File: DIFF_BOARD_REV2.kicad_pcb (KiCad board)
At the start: 2 copper layers, 101.6 x 82.6 mm, 44 parts, among them U100 DRV8212PDSGR, U101 DRV8212PDSGR, U103 SN65HVD230DR

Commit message: updated QR code on silkscreen to match github repository
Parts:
- moved G*** 5.60 mm to (193.7, 123.6)

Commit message: added fuse and made power nets thicker
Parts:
- added F100: Fuse, Fuse:Fuse_1206_3216Metric, F.Cu at (115.6, 70.1)
- moved D103 10.8 mm to (115.6, 80.2)
- renumbered CANH to CANH100, CANL to CANL100, RX to RX100, TX to TX100
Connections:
- D103 pad 2: /Enclosure Connectors/P+ -> Net-(D103-A)
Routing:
- net Motor_Power+: track 67.1 -> 56.4 mm
- net Net-(D103-A): track 0.00 -> 5.25 mm
- net /Enclosure Connectors/P+: track 13.3 -> 15.5 mm

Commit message: updated silkscreen
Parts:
- renumbered CANH100 to CANH, CANL100 to CANL, RX100 to RX, TX100 to TX

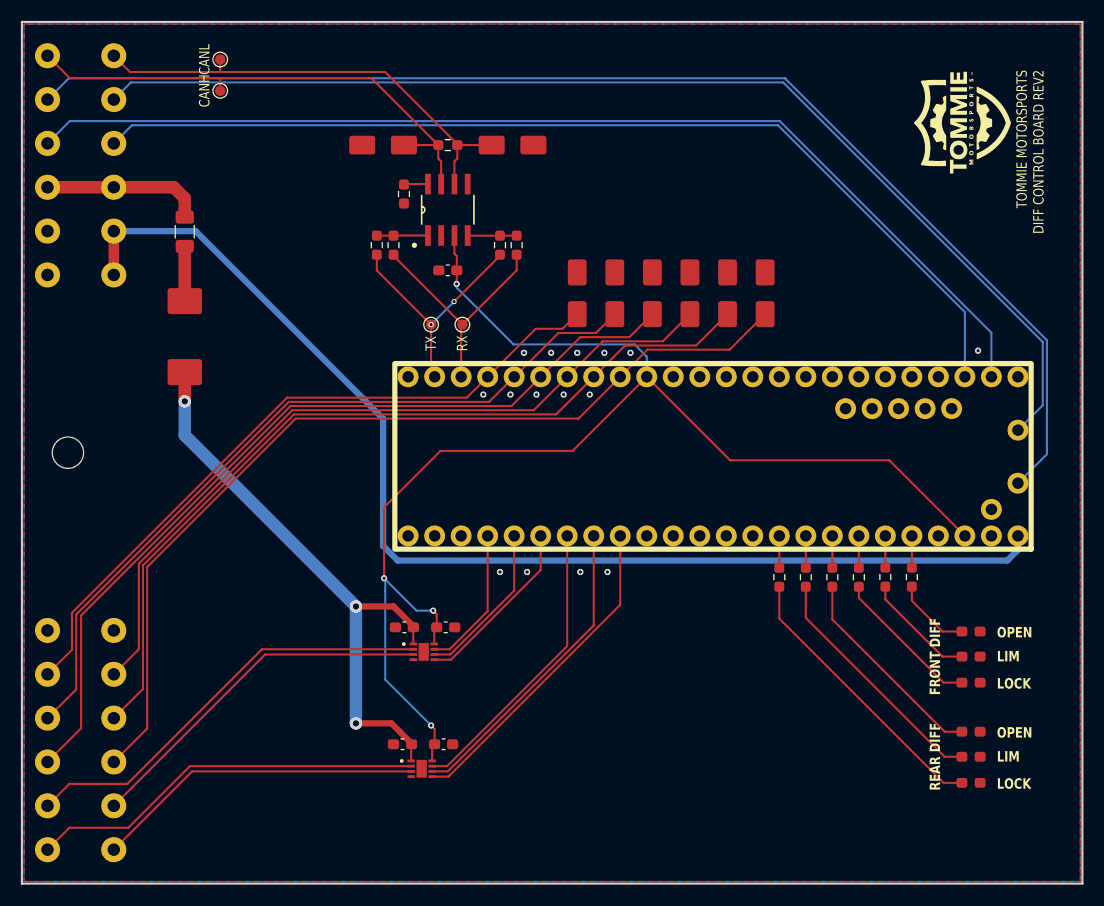
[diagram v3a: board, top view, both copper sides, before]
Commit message: larger silkscreen
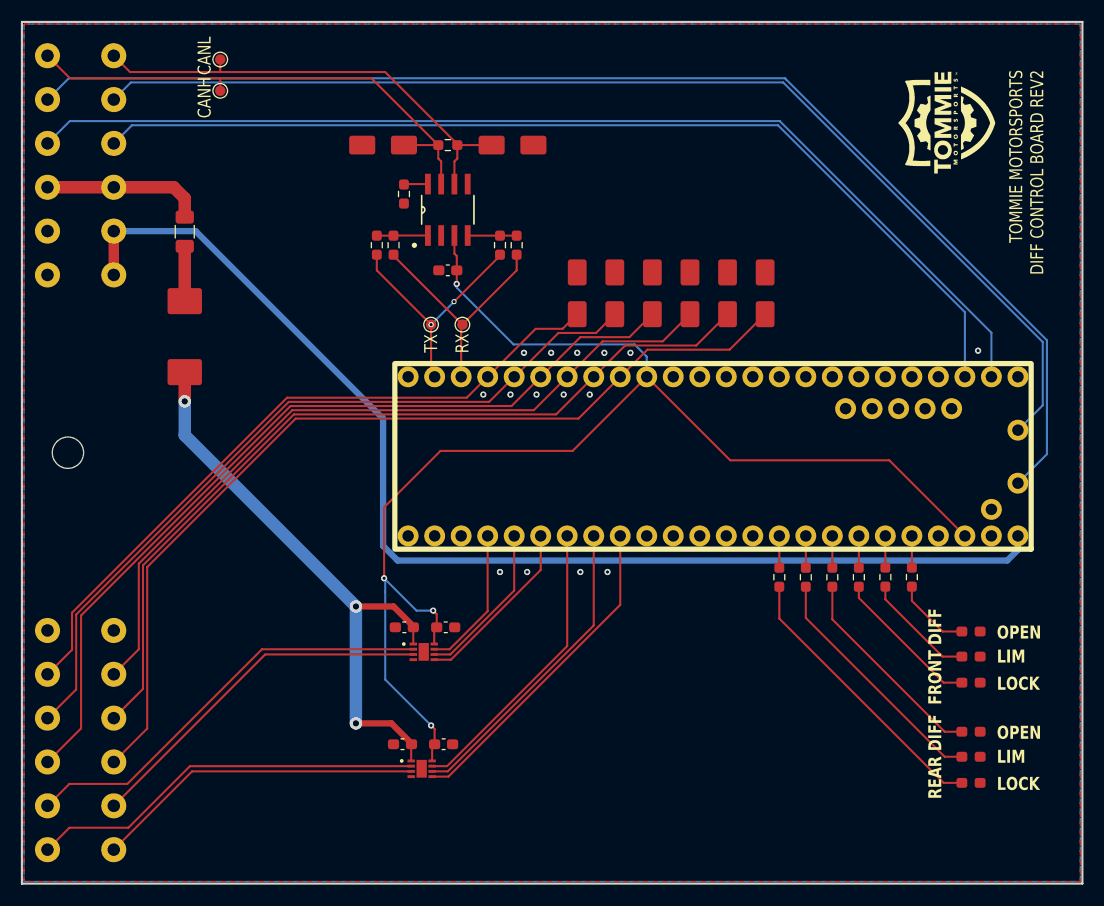
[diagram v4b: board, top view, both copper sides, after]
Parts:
- moved G*** 1.50 mm to (188.5, 59.6)
- moved G*** 0.60 mm to (189.5, 58.8)
